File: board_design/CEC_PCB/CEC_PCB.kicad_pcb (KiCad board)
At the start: 4 copper layers, 50 x 40 mm, 19 parts, among them J1 HDMI_A, J2 HDMI_A, J3 Conn_02x12_Odd_Even, J4 Conn_02x12_Odd_Even, J5 Conn_01x06_Pin, Q1 BSS138, U1 XC6206PxxxMR

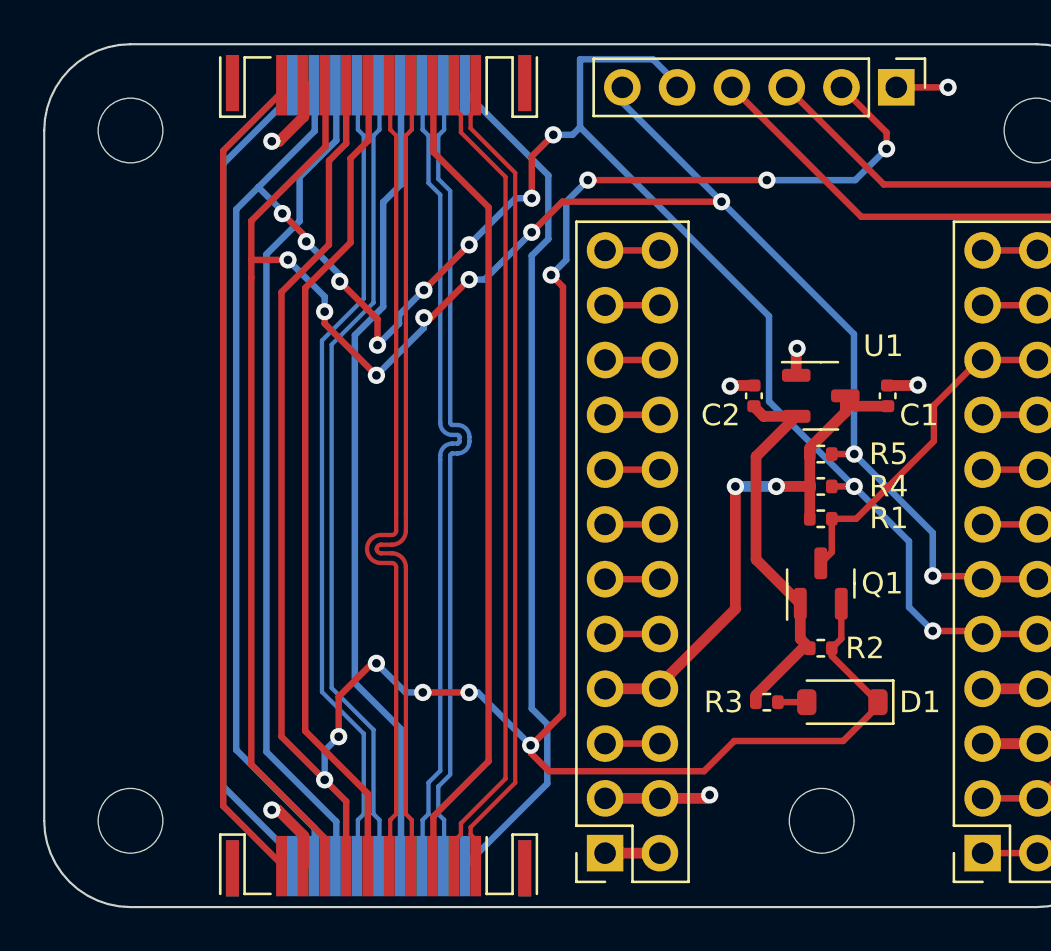
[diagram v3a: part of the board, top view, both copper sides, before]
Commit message: Optimizations and silkscreen annotations
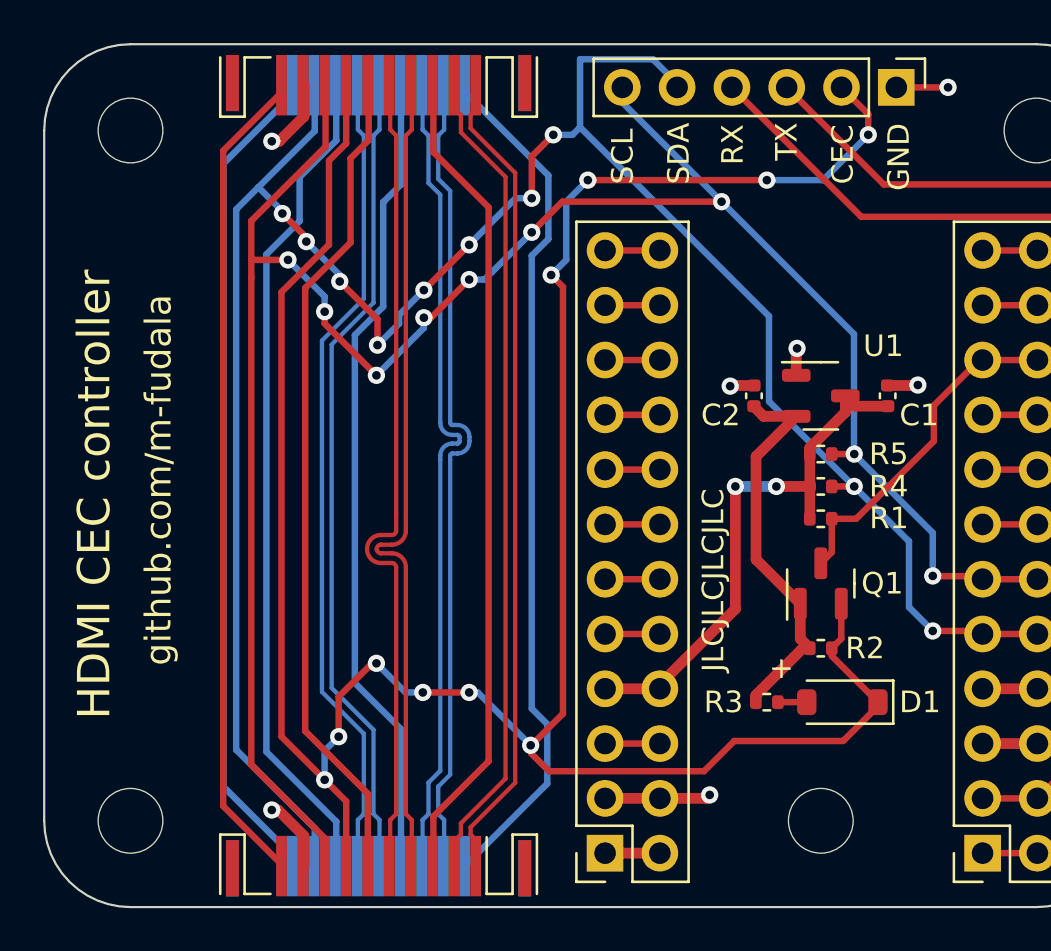
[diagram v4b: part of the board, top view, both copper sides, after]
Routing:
- net /CEC: track 124.3 -> 122.6 mm
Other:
- board text added: "+"
- board text added: "CEC"
- board text added: "GND"
- board text added: "HDMI CEC controller"
- board text added: "JLCJLCJLCJLC"
- board text added: "RX"
- board text added: "SCL"
- board text added: "SDA"
- board text added: "TX"
- board text added: "github.com/m-fudala"
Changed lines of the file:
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@@
       (usegerberattributes true)
       (usegerberadvancedattributes true)
-      (creategerberjobfile true)
+      (creategerberjobfile false)
       (dashed_line_dash_ratio 12.000000)
       (dashed_line_gap_ratio 3.000000)
@@
       (outputformat 1)
       (mirror false)
-      (drillshape 1)
+      (drillshape 0)
       (scaleselection 1)
-      (outputdirectory "")
+      (outputdirectory "manufacture/")
     )
   )
@@
   )
   (footprint "MountingHole:MountingHole_3mm" (layer "F.Cu")
-    (at 161.040049 111.5)
+    (at 161 111.5)
     (descr "Mounting Hole 3mm, no annular")
     (tags "mounting hole 3mm no annular")
@@
   (gr_line (start 125 111.5) (end 125 79.5)
     (stroke (width 0.1) (type default)) (layer "Edge.Cuts"))
+  (gr_text "GND" (at 165.2 82.3 90) (layer "F.SilkS" knockout)
+    (effects (font (size 1 1) (thickness 0.16)) (justify left bottom))
+  )
+  (gr_text "SDA" (at 155 82 90) (layer "F.SilkS")
+    (effects (font (size 1 1) (thickness 0.16)) (justify left bottom))
+  )
+  (gr_text "TX" (at 160 80.9 90) (layer "F.SilkS")
+    (effects (font (size 1 1) (thickness 0.16)) (justify left bottom))
+  )
+  (gr_text "+" (at 158.6 105) (layer "F.SilkS")
+    (effects (font (size 1 1) (thickness 0.16)) (justify left bottom))
+  )
+  (gr_text "JLCJLCJLCJLC" (at 156.6 104.6 90) (layer "F.SilkS")
+    (effects (font (size 1 1) (thickness 0.16)) (justify left bottom))
+  )
+  (gr_text "CEC" (at 162.6 82 90) (layer "F.SilkS")
+    (effects (font (size 1 1) (thickness 0.16)) (justify left bottom))
+  )
+  (gr_text "SCL" (at 152.4 82 90) (layer "F.SilkS")
+    (effects (font (size 1 1) (thickness 0.16)) (justify left bottom))
+  )
+  (gr_text "github.com/m-fudala" (at 131 95.7 90) (layer "F.SilkS")
+    (effects (font (size 1.2 1.2) (thickness 0.16)) (justify bottom))
+  )
+  (gr_text "HDMI CEC controller" (at 128.2 106.8 90) (layer "F.SilkS")
+    (effects (font (size 1.5 1.5) (thickness 0.15)) (justify left bottom))
+  )
+  (gr_text "RX" (at 157.5 81.1 90) (layer "F.SilkS")
+    (effects (font (size 1 1) (thickness 0.16)) (justify left bottom))
+  )
   (segment (start 161.51 103.86) (end 163.65 106) (width 0.3) (layer "F.Cu") (net 1))
   (segment (start 155.590049 109.2) (end 148.4 109.2) (width 0.3) (layer "F.Cu") (net 1))
@@
   (segment (start 139 77.4) (end 139 80.1) (width 0.3) (layer "F.Cu") (net 1))
   (segment (start 158.5 81.8) (end 150.2 81.8) (width 0.3) (layer "F.Cu") (net 1))
+  (segment (start 163.2 78.74) (end 161.96 77.5) (width 0.3) (layer "F.Cu") (net 1))
   (segment (start 136 107.6) (end 138 109.6) (width 0.3) (layer "F.Cu") (net 1))
   (segment (start 148.4 109.2) (end 147.570049 108.370049) (width 0.3) (layer "F.Cu") (net 1))
   (segment (start 144.480049 105.58) (end 144.490049 105.59) (width 0.3) (layer "F.Cu") (net 1))
-  (segment (start 164.05 79.59) (end 161.96 77.5) (width 0.3) (layer "F.Cu") (net 1))
   (segment (start 138.2 80.9) (end 138.2 84.792894) (width 0.3) (layer "F.Cu") (net 1))
   (segment (start 136 86.992894) (end 136 107.6) (width 0.3) (layer "F.Cu") (net 1))
@@
   (segment (start 147.570049 108.370049) (end 147.570049 108.01) (width 0.3) (layer "F.Cu") (net 1))
   (segment (start 161.51 103.5) (end 161.51 103.86) (width 0.3) (layer "F.Cu") (net 1))
-  (segment (start 164.05 80.35) (end 164.05 79.59) (width 0.3) (layer "F.Cu") (net 1))
   (segment (start 139 110.6) (end 138 109.6) (width 0.3) (layer "F.Cu") (net 1))
   (segment (start 163.65 106) (end 163.65 106.190049) (width 0.3) (layer "F.Cu") (net 1))
+  (segment (start 163.2 79.7) (end 163.2 78.74) (width 0.3) (layer "F.Cu") (net 1))
   (via (at 138 109.6) (size 0.8) (drill 0.4) (layers "F.Cu" "B.Cu") (net 1))
   (via (at 150.2 81.8) (size 0.8) (drill 0.4) (layers "F.Cu" "B.Cu") (net 1))
@@
   (via (at 158.5 81.8) (size 0.8) (drill 0.4) (layers "F.Cu" "B.Cu") (net 1))
   (via (at 138.65 107.6) (size 0.8) (drill 0.4) (layers "F.Cu" "B.Cu") (net 1))
-  (via (at 164.05 80.35) (size 0.8) (drill 0.4) (layers "F.Cu" "B.Cu") (net 1))
+  (via (at 163.2 79.7) (size 0.8) (drill 0.4) (layers "F.Cu" "B.Cu") (net 1))
   (segment (start 138 109.6) (end 138 108.25) (width 0.3) (layer "B.Cu") (net 1))
   (segment (start 148.5 86.2) (end 149.2 85.5) (width 0.3) (layer "B.Cu") (net 1))
   (segment (start 145.1 105.55) (end 147.55 108) (width 0.3) (layer "B.Cu") (net 1))
-  (segment (start 164.1 80.3) (end 164.05 80.35) (width 0.3) (layer "B.Cu") (net 1))
+  (segment (start 161.1 81.8) (end 163.2 79.7) (width 0.3) (layer "B.Cu") (net 1))
   (segment (start 149.2 85.5) (end 149.2 82.8) (width 0.3) (layer "B.Cu") (net 1))
+  (segment (start 158.5 81.8) (end 161.1 81.8) (width 0.3) (layer "B.Cu") (net 1))
   (segment (start 142.560049 105.59) (end 142.570049 105.58) (width 0.3) (layer "B.Cu") (net 1))
   (segment (start 144.7 105.55) (end 145.1 105.55) (width 0.3) (layer "B.Cu") (net 1))
   (segment (start 142.55 105.55) (end 141.75 105.55) (width 0.3) (layer "B.Cu") (net 1))
-  (segment (start 162.6 81.8) (end 164.05 80.35) (width 0.3) (layer "B.Cu") (net 1))
   (segment (start 138 108.25) (end 138.65 107.6) (width 0.3) (layer "B.Cu") (net 1))
-  (segment (start 158.5 81.8) (end 162.6 81.8) (width 0.3) (layer "B.Cu") (net 1))
   (segment (start 149.2 82.8) (end 150.2 81.8) (width 0.3) (layer "B.Cu") (net 1))
   (segment (start 141.75 105.55) (end 140.4 104.2) (width 0.3) (layer "B.Cu") (net 1))
@@
     (polygon
       (pts
-        (xy 125 115)
-        (xy 125 74)
-        (xy 176 74)
-        (xy 176 115)
+        (xy 125 115.5)
+        (xy 125 75.5)
+        (xy 175 75.5)
+        (xy 175 115.5)
       )
     )
@@
     (polygon
       (pts
-        (xy 125 74)
-        (xy 125 115)
-        (xy 176 115)
-        (xy 176 74)
+        (xy 125 75.5)
+        (xy 125 115.5)
+        (xy 175 115.5)
+        (xy 175 75.5)
       )
     )

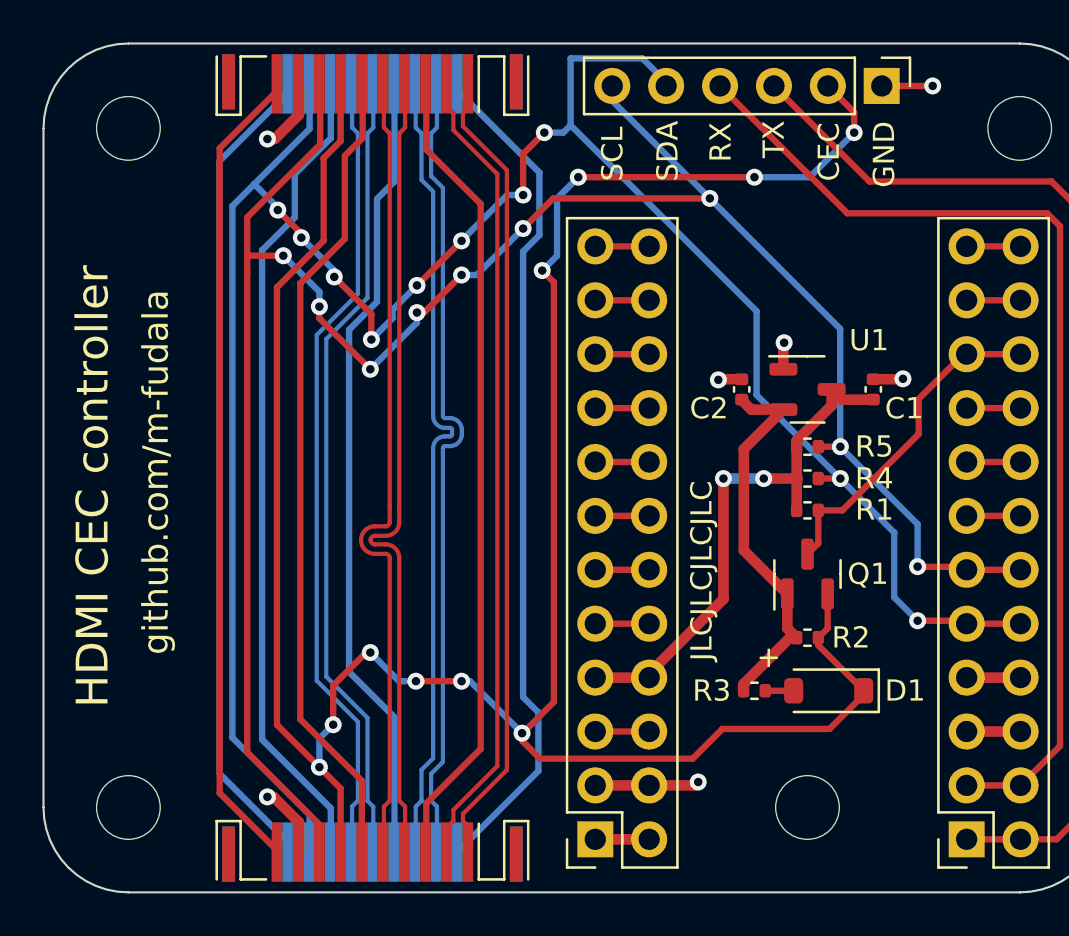
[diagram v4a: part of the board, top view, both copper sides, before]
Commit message: Changed VDO capacitors to 1uF Some routing changes Ground vias throughout the PCB Some optimizations
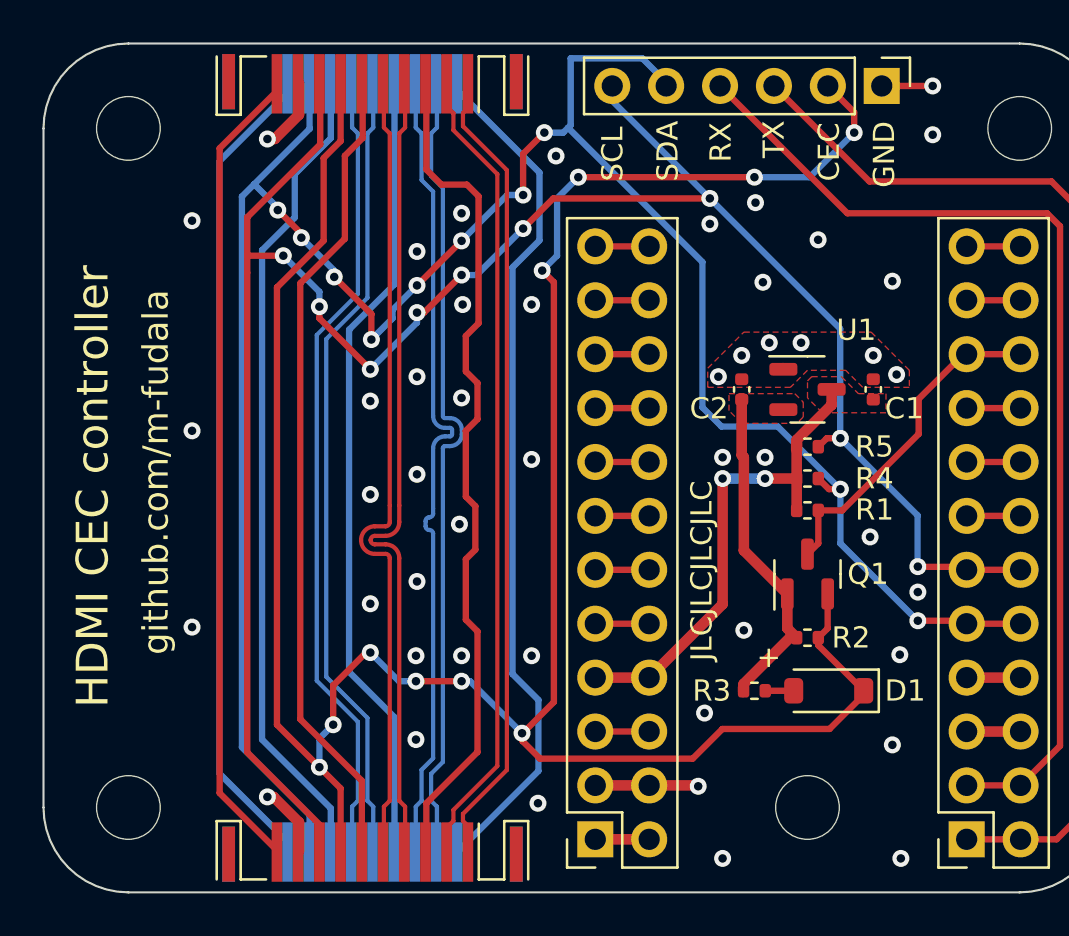
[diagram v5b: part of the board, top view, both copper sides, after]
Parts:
- C1, C2: value 0.1u -> 1u
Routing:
- net GND: track 23.3 -> 19.3 mm, vias 7 -> 48
- net +3V3: track 18.7 -> 16.3 mm
- net VCC: track 25.3 -> 23.1 mm
- net /D1S: track 38.3 -> 40.2 mm
- net /SDA: track 108.8 -> 110.1 mm
- added copper zone on F.Cu, net +3V3
- added copper zone on F.Cu, net GND
- added copper zone on F.Cu, net VCC
